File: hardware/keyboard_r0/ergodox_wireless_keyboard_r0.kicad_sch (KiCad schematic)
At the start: 0 parts

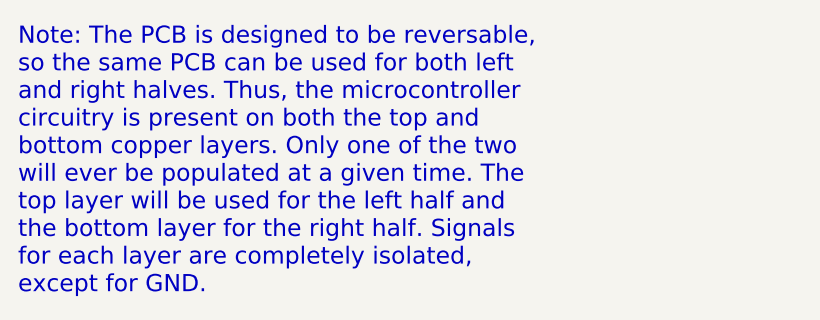
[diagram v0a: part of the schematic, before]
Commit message: Remove optional low-frequency oscillator circuit.
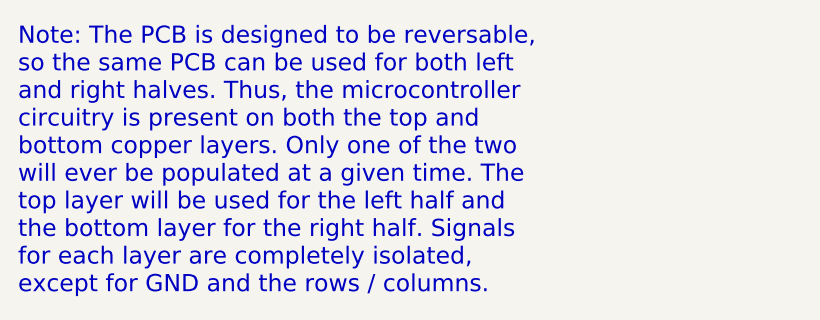
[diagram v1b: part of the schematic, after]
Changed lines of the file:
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@@
 		)
 	)
-	(text "Note: The PCB is designed to be reversable,\nso the same PCB can be used for both left\nand right halves. Thus, the microcontroller\ncircuitry is present on both the top and\nbottom copper layers. Only one of the two\nwill ever be populated at a given time. The\ntop layer will be used for the left half and\nthe bottom layer for the right half. Signals\nfor each layer are completely isolated,\nexcept for GND."
+	(text "Note: The PCB is designed to be reversable,\nso the same PCB can be used for both left\nand right halves. Thus, the microcontroller\ncircuitry is present on both the top and\nbottom copper layers. Only one of the two\nwill ever be populated at a given time. The\ntop layer will be used for the left half and\nthe bottom layer for the right half. Signals\nfor each layer are completely isolated,\nexcept for GND and the rows / columns."
 		(exclude_from_sim no)
 		(at 15.24 200.66 0)
